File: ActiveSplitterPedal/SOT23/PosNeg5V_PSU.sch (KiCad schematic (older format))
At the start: 14 parts, among them U3 TPS60400, U9 SE8250X2

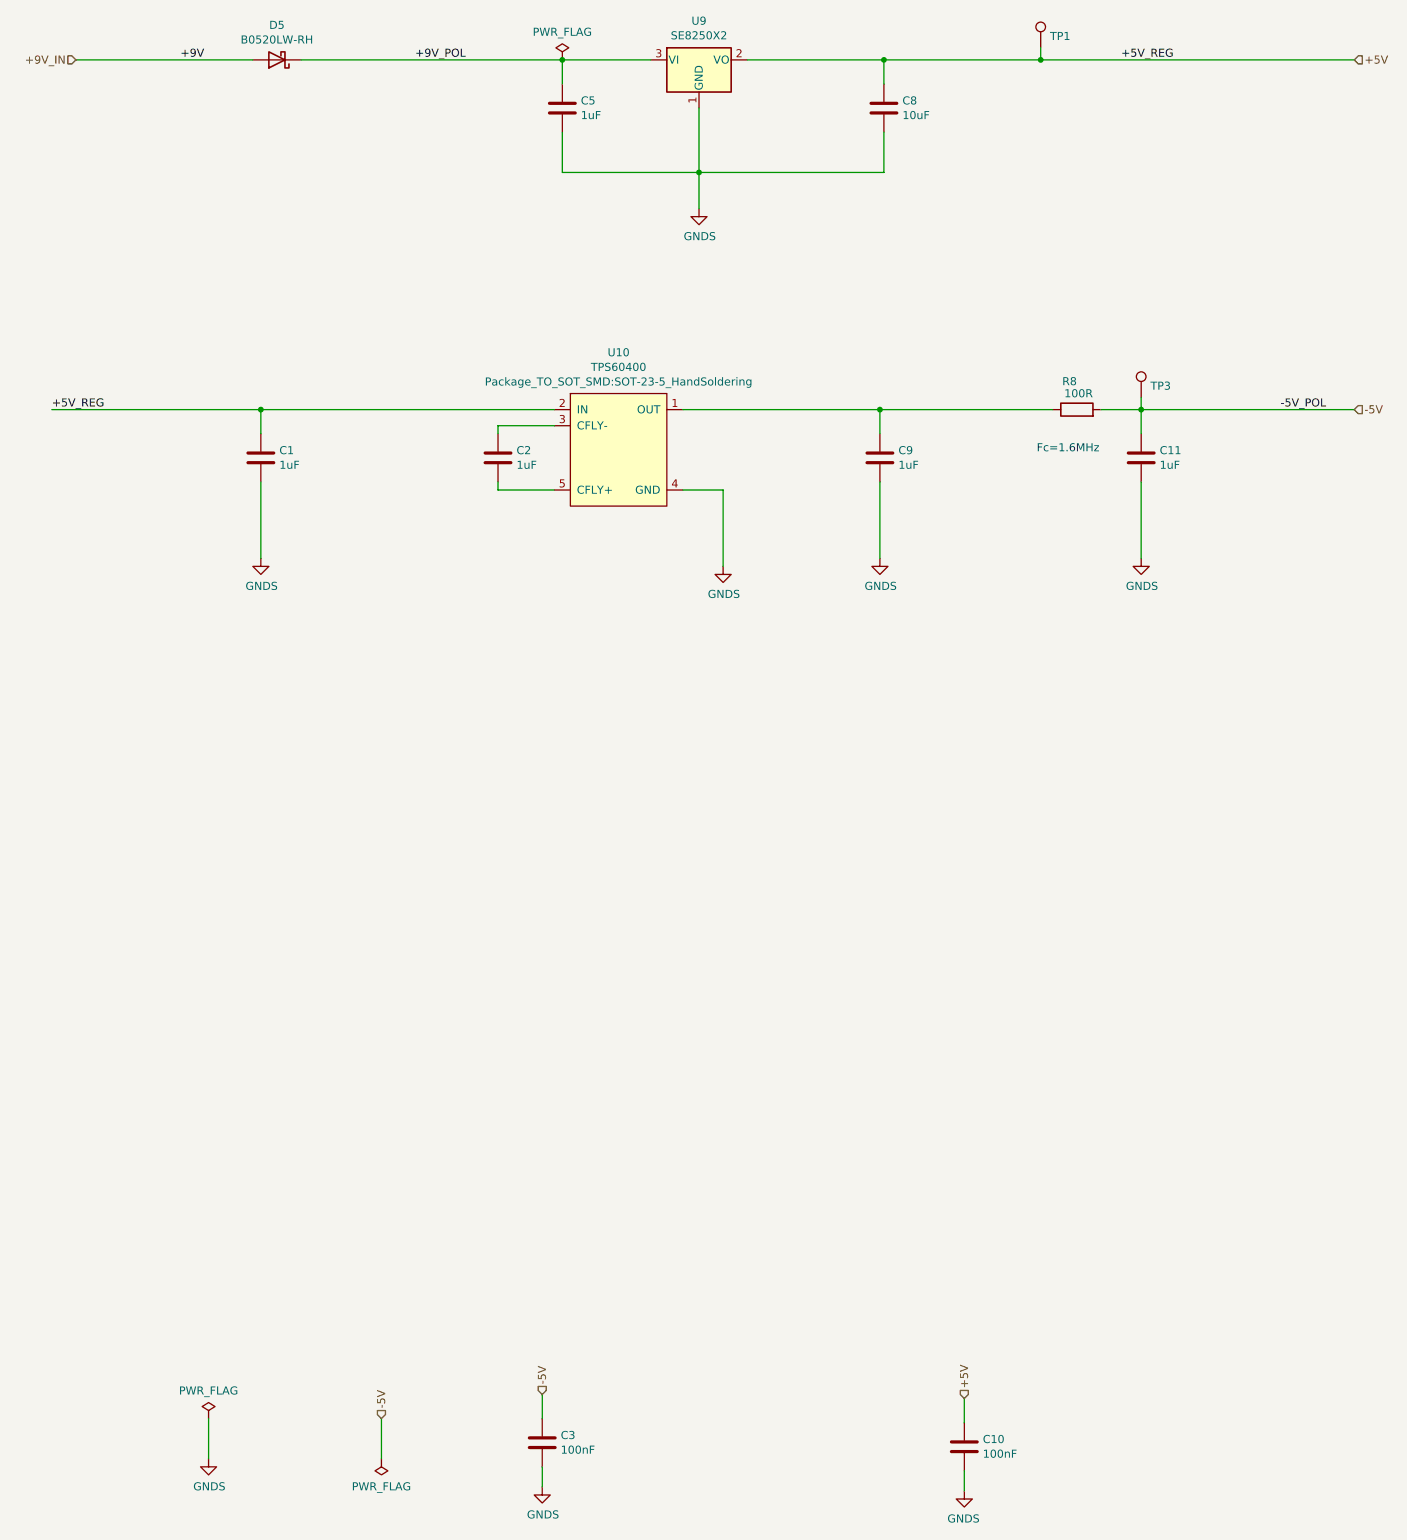
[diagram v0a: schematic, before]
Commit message: SOT23 REVA draft layout completed
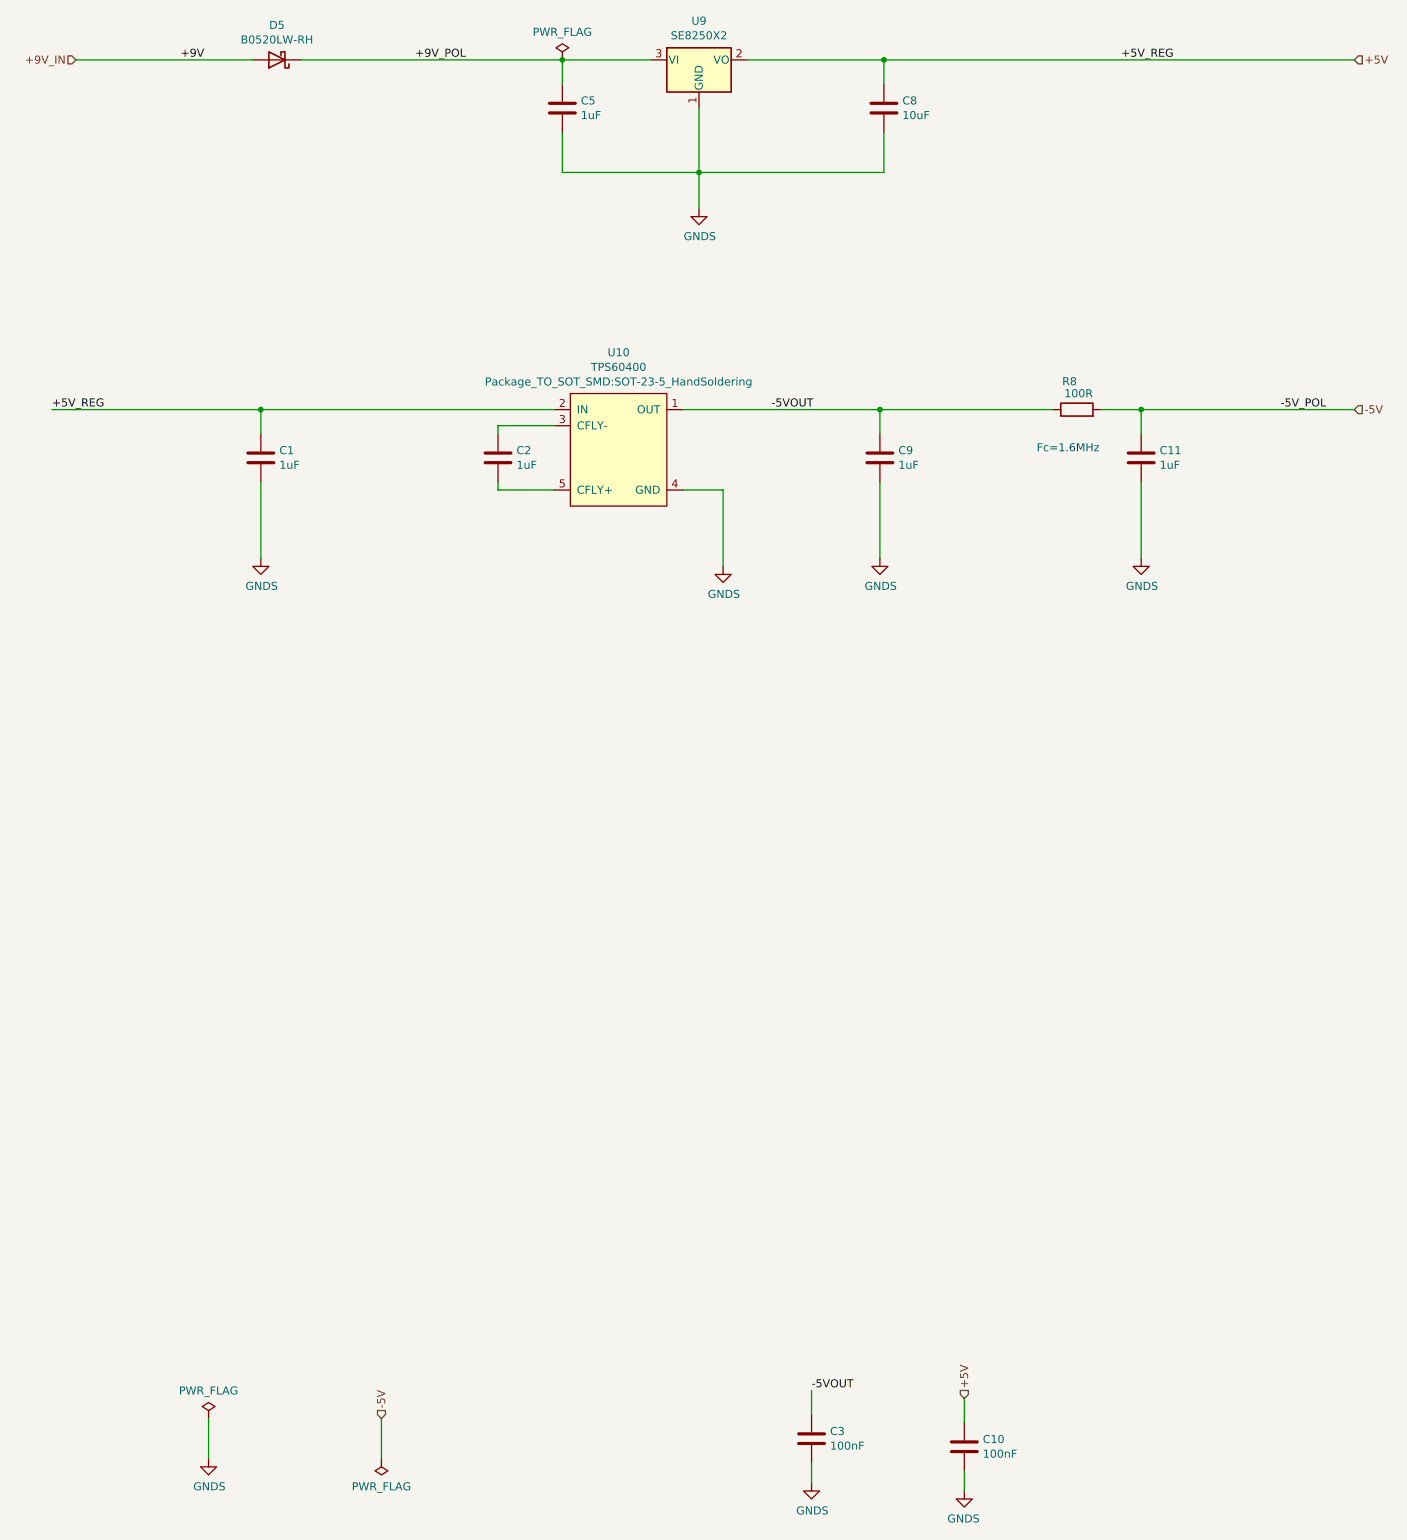
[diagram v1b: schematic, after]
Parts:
- removed TP1, TP3: TestPoint, TestPoint:TestPoint_Pad_1.0x1.0mm, symbol Connector:TestPoint
- C12, C13, C3, C4, C5, C6, C7: footprint Capacitor_SMD:C_0402_1005Metric -> Capacitor_SMD:C_0805_2012Metric_Pad1.15x1.40mm_HandSolder
- R7: footprint Resistor_SMD:R_0402_1005Metric -> Resistor_SMD:R_0805_2012Metric_Pad1.15x1.40mm_HandSolder
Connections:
- net -5V: no longer C7.1
- net -5VOUT: now reaches C5.1, R7.1, U3.1 (OUT)
- net -5VOUT: now also C7.1
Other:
- moved on the sheet: C3
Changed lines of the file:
@@
 F 0 "C2" H 6515 4196 50  0000 L CNN
 F 1 "1uF" H 6515 4105 50  0000 L CNN
-F 2 "Capacitor_SMD:C_0402_1005Metric" H 6438 4000 50  0001 C CNN
+F 2 "Capacitor_SMD:C_0805_2012Metric_Pad1.15x1.40mm_HandSolder" H 6438 4000 50  0001 C CNN
 F 3 "~" H 6400 4150 50  0001 C CNN
 	1    6400 4150
@@
 F 0 "C1" H 5040 4196 50  0000 L CNN
 F 1 "1uF" H 5040 4105 50  0000 L CNN
-F 2 "Capacitor_SMD:C_0402_1005Metric" H 4963 4000 50  0001 C CNN
+F 2 "Capacitor_SMD:C_0805_2012Metric_Pad1.15x1.40mm_HandSolder" H 4963 4000 50  0001 C CNN
 F 3 "~" H 4925 4150 50  0001 C CNN
 	1    4925 4150
@@
 F 0 "C9" H 8890 4196 50  0000 L CNN
 F 1 "1uF" H 8890 4105 50  0000 L CNN
-F 2 "Capacitor_SMD:C_0402_1005Metric" H 8813 4000 50  0001 C CNN
+F 2 "Capacitor_SMD:C_0805_2012Metric_Pad1.15x1.40mm_HandSolder" H 8813 4000 50  0001 C CNN
 F 3 "~" H 8775 4150 50  0001 C CNN
 	1    8775 4150
@@
 F 0 "C8" H 8915 2021 50  0000 L CNN
 F 1 "10uF" H 8915 1930 50  0000 L CNN
-F 2 "Capacitor_SMD:C_0402_1005Metric" H 8838 1825 50  0001 C CNN
+F 2 "Capacitor_SMD:C_0805_2012Metric_Pad1.15x1.40mm_HandSolder" H 8838 1825 50  0001 C CNN
 F 3 "~" H 8800 1975 50  0001 C CNN
 	1    8800 1975
@@
 	6800 1675 7350 1675
 Connection ~ 8800 1675
-Wire Wire Line
-	8800 1675 9775 1675
 Text Label 10275 1675 0    50   ~ 0
 +5V_REG
@@
 F 0 "C11" H 10515 4196 50  0000 L CNN
 F 1 "1uF" H 10515 4105 50  0000 L CNN
-F 2 "Capacitor_SMD:C_0402_1005Metric" H 10438 4000 50  0001 C CNN
+F 2 "Capacitor_SMD:C_0805_2012Metric_Pad1.15x1.40mm_HandSolder" H 10438 4000 50  0001 C CNN
 F 3 "~" H 10400 4150 50  0001 C CNN
 	1    10400 4150
@@
 F 0 "R8" V 10175 3850 50  0000 L CNN
 F 1 "100R" V 10100 3750 50  0000 L CNN
-F 2 "Resistor_SMD:R_0402_1005Metric" V 9930 3850 50  0001 C CNN
+F 2 "Resistor_SMD:R_0805_2012Metric_Pad1.15x1.40mm_HandSolder" V 9930 3850 50  0001 C CNN
 F 3 "~" H 10000 3850 50  0001 C CNN
 	1    10000 3850
@@
 L Device:C C7
 U 1 1 5EB4CD19
-P 6675 10275
+P 8350 10250
 AR Path="/5E6165F4/5EB4CD19" Ref="C7"  Part="1"
 AR Path="/5E6A8284/5EB4CD19" Ref="C?"  Part="1"
 AR Path="/5EB4CD19" Ref="C?"  Part="1"
 AR Path="/5F3902BC/5EB4CD19" Ref="C3"  Part="1"
-F 0 "C3" H 6790 10321 50  0000 L CNN
-F 1 "100nF" H 6790 10230 50  0000 L CNN
-F 2 "Capacitor_SMD:C_0402_1005Metric" H 6713 10125 50  0001 C CNN
-F 3 "~" H 6675 10275 50  0001 C CNN
-	1    6675 10275
-	1    0    0    -1
-$EndComp
-Wire Wire Line
-	6675 10425 6675 10550
+F 0 "C3" H 8465 10296 50  0000 L CNN
+F 1 "100nF" H 8465 10205 50  0000 L CNN
+F 2 "Capacitor_SMD:C_0805_2012Metric_Pad1.15x1.40mm_HandSolder" H 8388 10100 50  0001 C CNN
+F 3 "~" H 8350 10250 50  0001 C CNN
+	1    8350 10250
+	1    0    0    -1
+$EndComp
+Wire Wire Line
+	8350 10400 8350 10525
 $Comp
 L power:GNDS #PWR018
 U 1 1 5EB4CD20
-P 6675 10550
+P 8350 10525
 AR Path="/5E6165F4/5EB4CD20" Ref="#PWR018"  Part="1"
 AR Path="/5EB4CD20" Ref="#PWR?"  Part="1"
 AR Path="/5F3902BC/5EB4CD20" Ref="#PWR026"  Part="1"
-F 0 "#PWR026" H 6675 10300 50  0001 C CNN
-F 1 "GNDS" H 6680 10377 50  0000 C CNN
-F 2 "" H 6675 10550 50  0001 C CNN
-F 3 "" H 6675 10550 50  0001 C CNN
-	1    6675 10550
+F 0 "#PWR026" H 8350 10275 50  0001 C CNN
+F 1 "GNDS" H 8355 10352 50  0000 C CNN
+F 2 "" H 8350 10525 50  0001 C CNN
+F 3 "" H 8350 10525 50  0001 C CNN
+	1    8350 10525
 	1    0    0    -1
 $EndComp
@@
 F 0 "C10" H 9415 10346 50  0000 L CNN
 F 1 "100nF" H 9415 10255 50  0000 L CNN
-F 2 "Capacitor_SMD:C_0402_1005Metric" H 9338 10150 50  0001 C CNN
+F 2 "Capacitor_SMD:C_0805_2012Metric_Pad1.15x1.40mm_HandSolder" H 9338 10150 50  0001 C CNN
 F 3 "~" H 9300 10300 50  0001 C CNN
 	1    9300 10300
@@
 	9300 10000 9300 10150
 Wire Wire Line
-	6675 9975 6675 10125
+	8350 9950 8350 10100
 $Comp
 L power:PWR_FLAG #FLG02
@@
 Wire Wire Line
 	5675 10375 5675 10125
-Text HLabel 6675 9975 1    50   Input ~ 0
+Text HLabel 5675 10125 1    50   Input ~ 0
 -5V
+Wire Wire Line
+	5175 1675 6800 1675
+Wire Wire Line
+	8800 1675 11725 1675
 Text HLabel 9300 10000 1    50   Input ~ 0
 +5V
-Text HLabel 5675 10125 1    50   Input ~ 0
--5V
-$Comp
-L Connector:TestPoint TP1
-U 1 1 5E835E7F
-P 9775 1600
-F 0 "TP1" H 9833 1672 50  0000 L CNN
-F 1 "TestPoint" H 9833 1627 50  0001 L CNN
-F 2 "TestPoint:TestPoint_Pad_1.0x1.0mm" H 9975 1600 50  0001 C CNN
-F 3 "~" H 9975 1600 50  0001 C CNN
-	1    9775 1600
-	1    0    0    -1
-$EndComp
-Wire Wire Line
-	9775 1600 9775 1675
-Connection ~ 9775 1675
-Wire Wire Line
-	9775 1675 11725 1675
-$Comp
-L Connector:TestPoint TP3
-U 1 1 5E83A778
-P 10400 3775
-F 0 "TP3" H 10458 3847 50  0000 L CNN
-F 1 "TestPoint" H 10458 3802 50  0001 L CNN
-F 2 "TestPoint:TestPoint_Pad_1.0x1.0mm" H 10600 3775 50  0001 C CNN
-F 3 "~" H 10600 3775 50  0001 C CNN
-	1    10400 3775
-	1    0    0    -1
-$EndComp
-Wire Wire Line
-	10400 3775 10400 3850
-Wire Wire Line
-	5175 1675 6800 1675
+Text Label 8100 3850 0    50   ~ 0
+-5VOUT
+Text Label 8350 9950 0    50   ~ 0
+-5VOUT
 $EndSCHEMATC

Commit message: Completed RevA layout
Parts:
- D5: footprint Diode_SMD:D_SOD-123F -> Diode_SMD:D_SMB_Handsoldering
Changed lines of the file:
@@
 F 0 "D5" H 5025 1459 50  0000 C CNN
 F 1 "B0520LW-RH" H 5025 1550 50  0000 C CNN
-F 2 "Diode_SMD:D_SOD-123F" H 5025 1675 50  0001 C CNN
+F 2 "Diode_SMD:D_SMB_Handsoldering" H 5025 1675 50  0001 C CNN
 F 3 "https://www.taiwansemi.com/products/datasheet/B0520LW%20SERIES_I1601.pdf" H 5025 1675 50  0001 C CNN
 	1    5025 1675
